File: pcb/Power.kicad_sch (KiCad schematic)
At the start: 95 parts, among them J4 Barrel_Jack, U4 LTC4360-1, U5 SI1416EDH

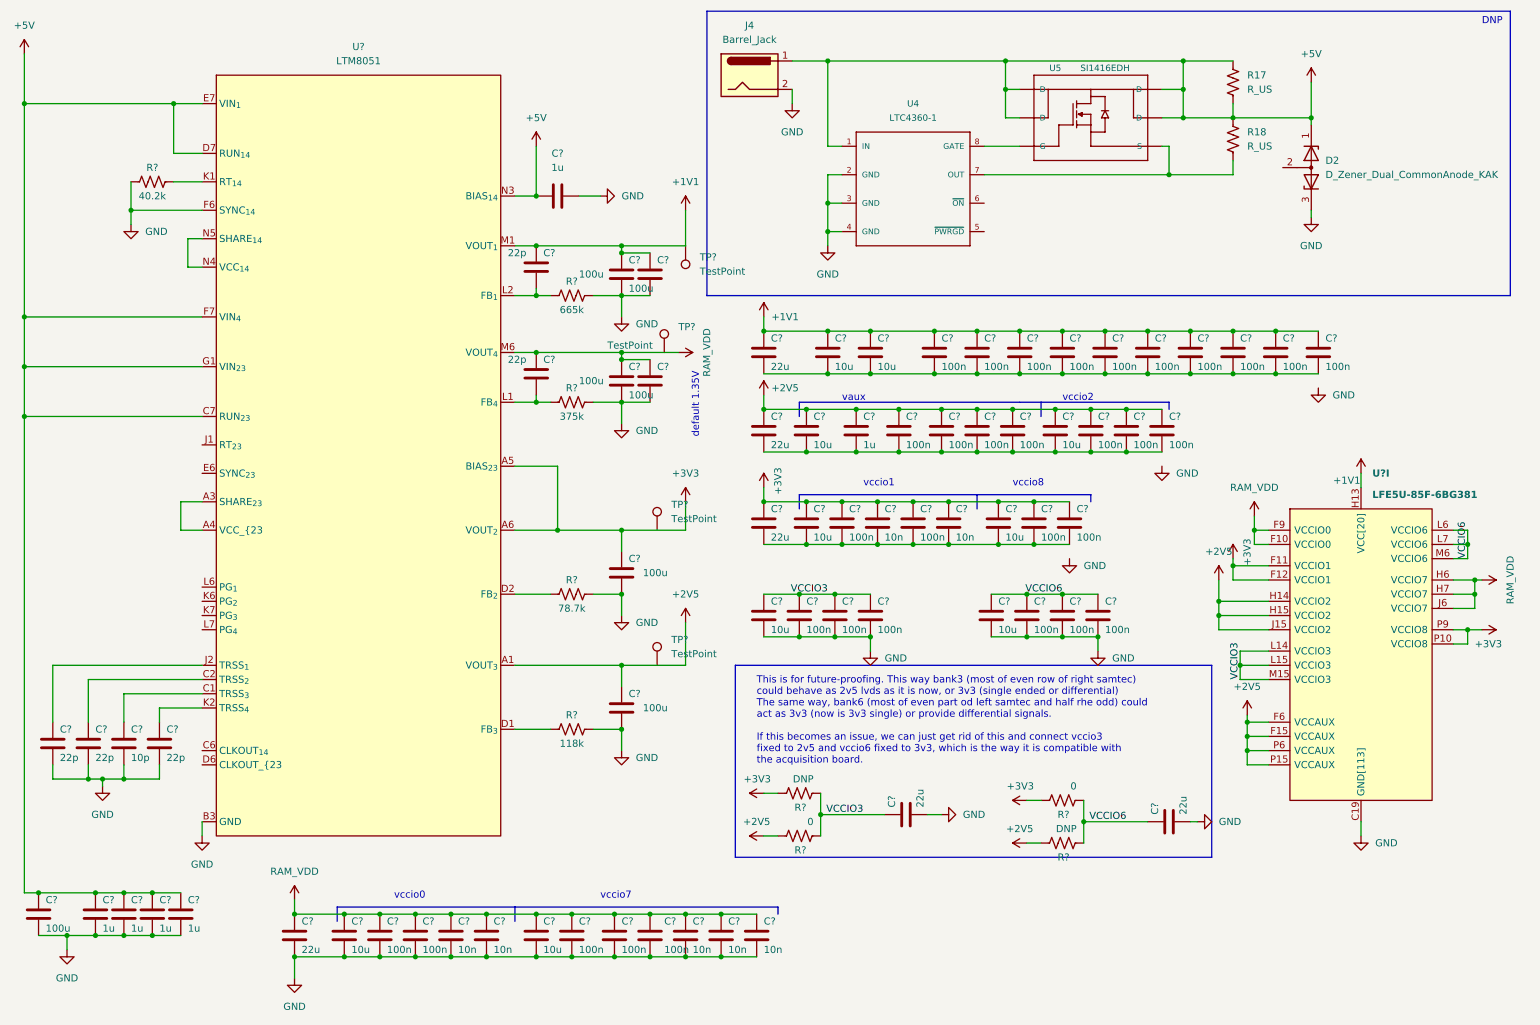
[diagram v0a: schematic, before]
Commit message: Fix some ERC errors
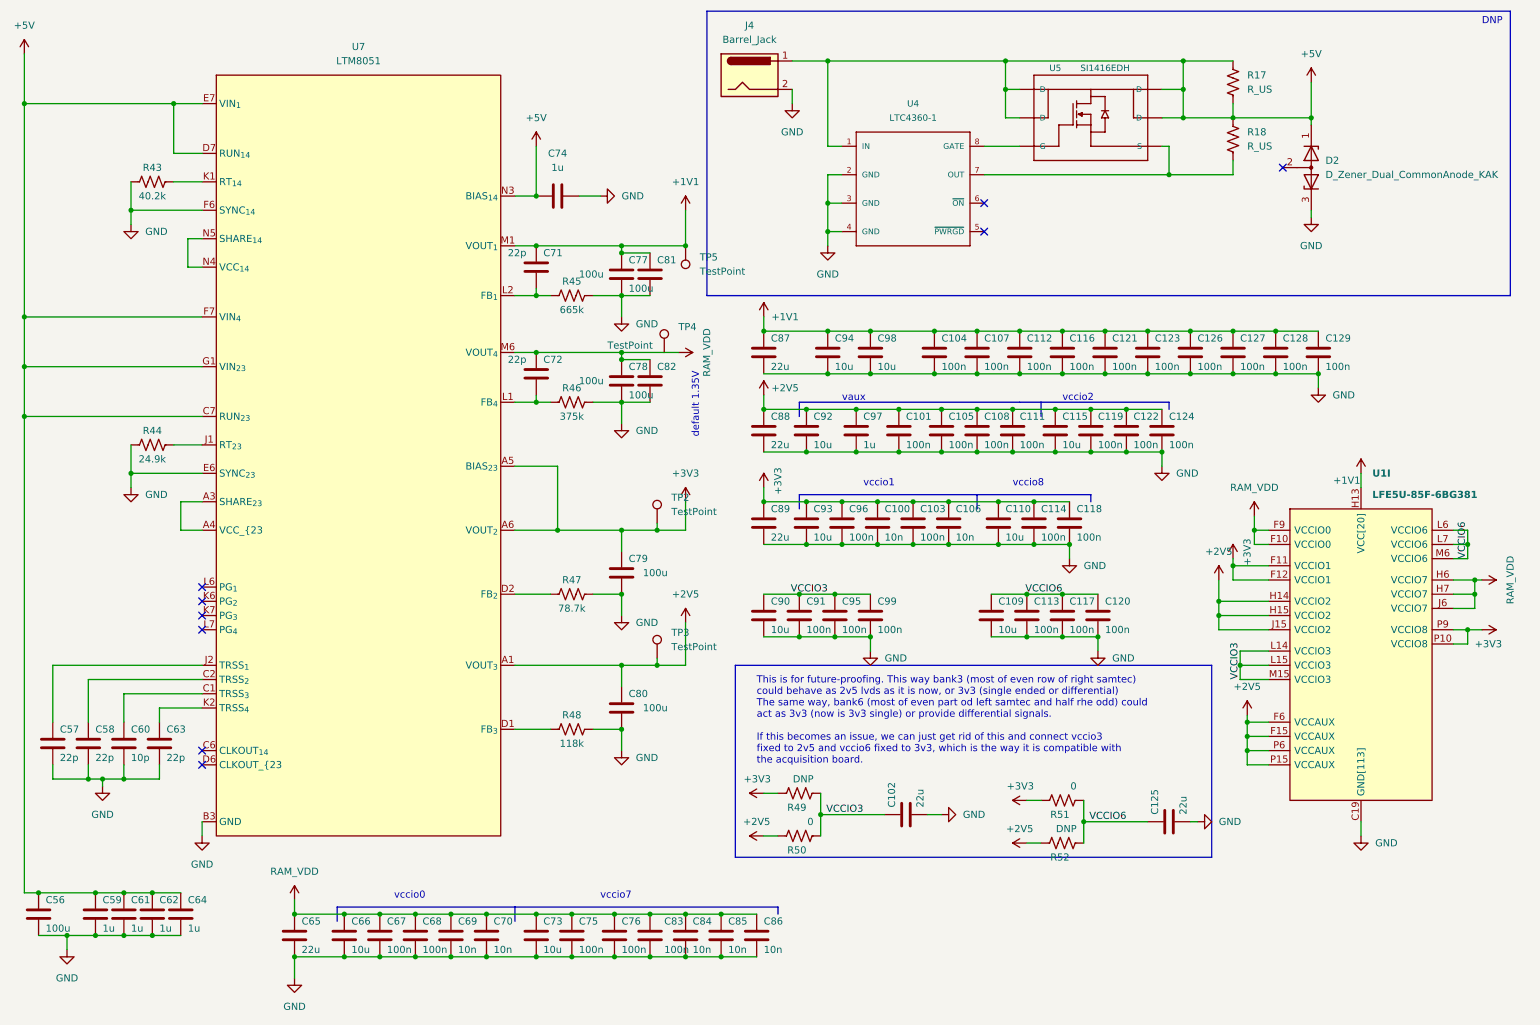
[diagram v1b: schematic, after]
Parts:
- added R44: 24.9k, symbol Device:R_US
- gave numbers to parts that had none: 89
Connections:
- net +2V5: now also TP3.1
- net +3V3: now also TP2.1
- net GND: now also C100.2, C101.2, C103.2, C104.2, C105.2, C106.2, C107.2, C108.2, C110.2, C111.2, C112.2, C114.2, C115.2, C116.2, C118.2, C119.2, C121.2, C122.2, C123.2, C124.2, C126.2, C127.2, C128.2, C129.2, C87.2, C88.2, C89.2, C92.2, C93.2, C94.2, C96.2, C97.2, C98.2, U7.E6 (SYNC_{23}), R44.1
- net at U7.J1 (RT_{23}): now also R44.2
- no-connect marks 0 -> 9
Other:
- moved on the sheet: TP2, TP3

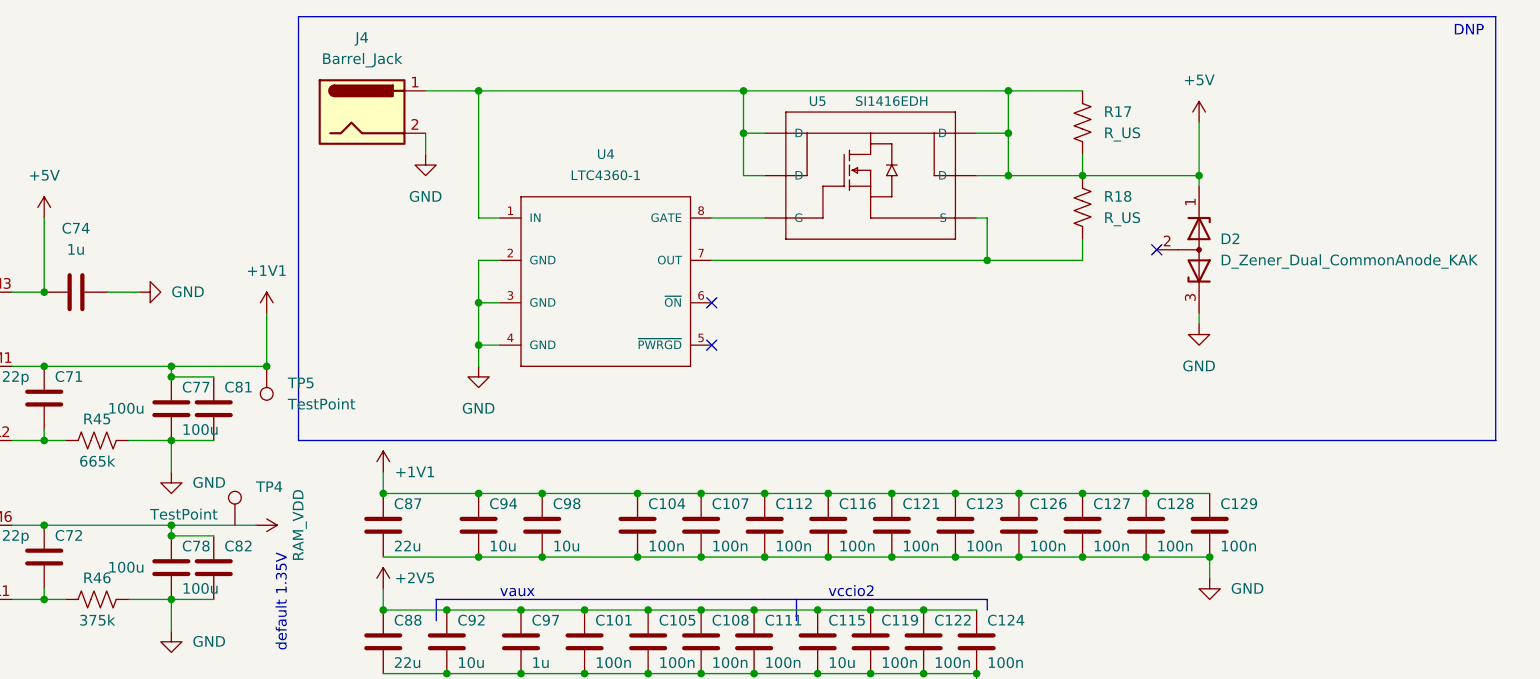
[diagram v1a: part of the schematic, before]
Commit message: Add filter and ESD protection to USB inputs
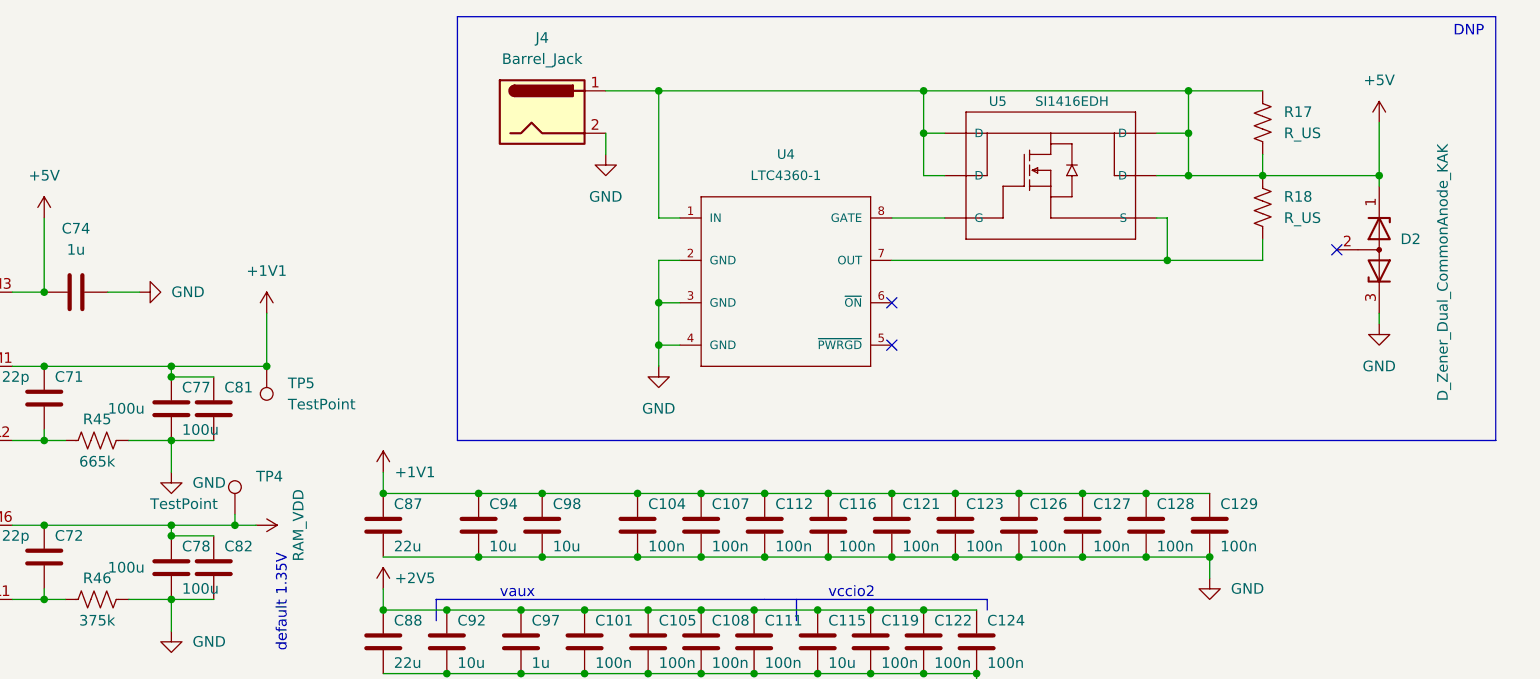
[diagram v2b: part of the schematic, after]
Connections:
- net RAM_VDD: now also TP4.1
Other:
- moved on the sheet: D2, J4, R17, R18, TP4, U4, U5

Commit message: Fix some symbols
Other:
- moved on the sheet: C125, R51, R52

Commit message: Some extra fixes and notes
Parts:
- R17: value R_US -> DNP
- R18: value R_US -> 0
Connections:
- net +5V: no longer J4.1, R17.1, U4.1 (IN), U5.1 (D), U5.2 (D), U5.5 (D), U5.6 (D)
- new net: J4.1, R17.1, U4.1 (IN), U5.1 (D), U5.2 (D), U5.5 (D), U5.6 (D)
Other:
- note added: "Ask Filipe"
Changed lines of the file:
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@@
   (junction (at 81.28 182.88) (diameter 0) (color 0 0 0 0)
   )
-  (junction (at 246.38 33.02) (diameter 0) (color 0 0 0 0)
-  )
   (junction (at 74.93 175.26) (diameter 0) (color 0 0 0 0)
   )
@@
     (stroke (width 0) (type default) (color 0 0 0 0))
   )
-  (wire (pts (xy 246.38 33.02) (xy 255.27 33.02))
-    (stroke (width 0) (type default) (color 0 0 0 0))
-  )
   (wire (pts (xy 203.2 71.12) (xy 210.82 71.12))
     (stroke (width 0) (type default) (color 0 0 0 0))
@@
     (effects (font (size 1.27 1.27)) (justify left bottom))
   )
+  (text "Ask Filipe" (at 256.54 31.75 0)
+    (effects (font (size 1.27 1.27)) (justify left bottom))
+  )
   (label "VCCIO3" (at 167.64 157.48 180)
     (effects (font (size 1.27 1.27)) (justify right bottom))
@@
       (effects (font (size 1.27 1.27)) (justify left))
     )
-    (property "Value" "R_US" (id 1) (at 257.81 38.0999 0)
+    (property "Value" "0" (id 1) (at 257.81 38.0999 0)
       (effects (font (size 1.27 1.27)) (justify left))
     )
@@
       (effects (font (size 1.27 1.27)) (justify left))
     )
-    (property "Value" "R_US" (id 1) (at 257.81 27.9399 0)
+    (property "Value" "DNP" (id 1) (at 257.81 27.9399 0)
       (effects (font (size 1.27 1.27)) (justify left))
     )
